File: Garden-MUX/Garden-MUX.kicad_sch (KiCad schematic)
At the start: 53 parts, among them J1 USB_C_Receptacle_USB2.0_16P, J2 SDCARD_MODULE, P1 S2B-PH-SM4-TB, Q1 AO3401A, U2 MCP73832-2-OT, U3 AP2112K-3.3, U4 AP2112K-3.3, U5 ESP32-C6-MINI-1

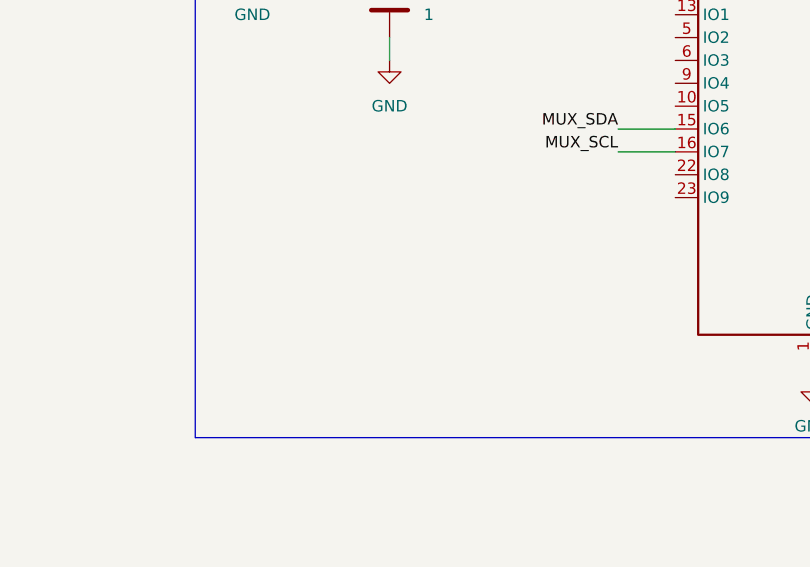
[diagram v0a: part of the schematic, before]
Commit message: Transfer capacitors from 4 layer board
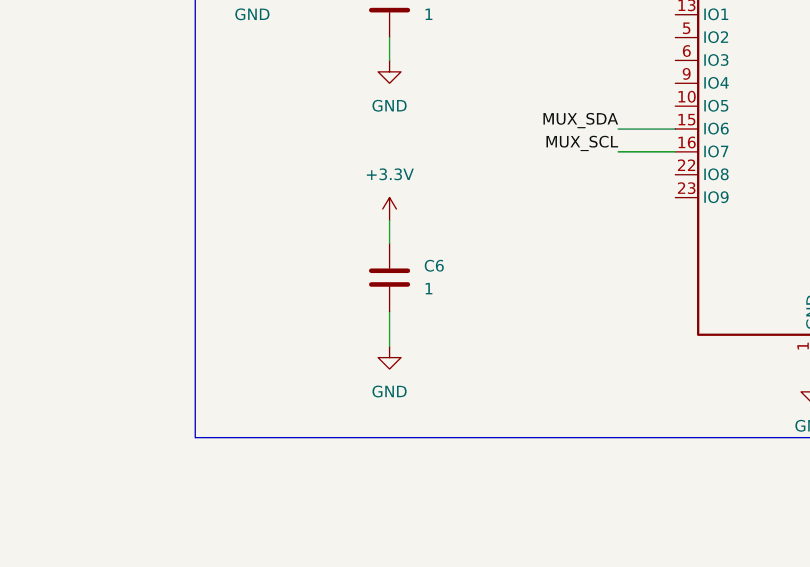
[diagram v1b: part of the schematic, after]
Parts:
- added C6: 1, Capacitor_SMD:C_0603_1608Metric, symbol Device:C
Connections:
- net +3.3V: now also C6.1
- net GND: now also C6.2
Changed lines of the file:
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@@
 	(wire
 		(pts
+			(xy 293.37 78.74) (xy 293.37 81.28)
+		)
+		(stroke
+			(width 0)
+			(type default)
+		)
+	)
+	(wire
+		(pts
 			(xy 417.83 58.42) (xy 417.83 68.58)
 		)
@@
 	(wire
 		(pts
+			(xy 293.37 88.9) (xy 293.37 92.71)
+		)
+		(stroke
+			(width 0)
+			(type default)
+		)
+	)
+	(wire
+		(pts
 			(xy 102.87 113.03) (xy 106.68 113.03)
 		)
@@
 	)
 	(symbol
+		(lib_id "power:GND")
+		(at 293.37 92.71 0)
+		(unit 1)
+		(exclude_from_sim no)
+		(in_bom yes)
+		(on_board yes)
+		(dnp no)
+		(fields_autoplaced yes)
+		(property "Reference" "#PWR039"
+			(at 293.37 99.06 0)
+			(effects
+				(font
+					(size 1.27 1.27)
+				)
+				(hide yes)
+			)
+		)
+		(property "Value" "GND"
+			(at 293.37 97.79 0)
+			(effects
+				(font
+					(size 1.27 1.27)
+				)
+			)
+		)
+		(property "Footprint" ""
+			(at 293.37 92.71 0)
+			(effects
+				(font
+					(size 1.27 1.27)
+				)
+				(hide yes)
+			)
+		)
+		(property "Datasheet" ""
+			(at 293.37 92.71 0)
+			(effects
+				(font
+					(size 1.27 1.27)
+				)
+				(hide yes)
+			)
+		)
+		(property "Description" "Power symbol creates a global label with name \"GND\" , ground"
+			(at 293.37 92.71 0)
+			(effects
+				(font
+					(size 1.27 1.27)
+				)
+				(hide yes)
+			)
+		)
+		(pin "1"
+		)
+		(instances
+			(project "Garden-MUX"
+				(path "/27ca7141-07bc-42d4-b74a-f55a9e480797"
+					(reference "#PWR039")
+					(unit 1)
+				)
+			)
+		)
+	)
+	(symbol
 		(lib_id "Mechanical:MountingHole")
 		(at 148.59 144.78 0)
@@
 	)
 	(symbol
+		(lib_id "power:+3V3")
+		(at 293.37 78.74 0)
+		(unit 1)
+		(exclude_from_sim no)
+		(in_bom yes)
+		(on_board yes)
+		(dnp no)
+		(fields_autoplaced yes)
+		(property "Reference" "#PWR040"
+			(at 293.37 82.55 0)
+			(effects
+				(font
+					(size 1.27 1.27)
+				)
+				(hide yes)
+			)
+		)
+		(property "Value" "+3.3V"
+			(at 293.37 73.66 0)
+			(effects
+				(font
+					(size 1.27 1.27)
+				)
+			)
+		)
+		(property "Footprint" ""
+			(at 293.37 78.74 0)
+			(effects
+				(font
+					(size 1.27 1.27)
+				)
+				(hide yes)
+			)
+		)
+		(property "Datasheet" ""
+			(at 293.37 78.74 0)
+			(effects
+				(font
+					(size 1.27 1.27)
+				)
+				(hide yes)
+			)
+		)
+		(property "Description" "Power symbol creates a global label with name \"+3V3\""
+			(at 293.37 78.74 0)
+			(effects
+				(font
+					(size 1.27 1.27)
+				)
+				(hide yes)
+			)
+		)
+		(pin "1"
+		)
+		(instances
+			(project "Garden-MUX"
+				(path "/27ca7141-07bc-42d4-b74a-f55a9e480797"
+					(reference "#PWR040")
+					(unit 1)
+				)
+			)
+		)
+	)
+	(symbol
 		(lib_id "power:GND")
 		(at 46.99 116.84 0)
@@
 					(unit 1)
 				)
+			)
+		)
+	)
+	(symbol
+		(lib_id "Device:C")
+		(at 293.37 85.09 0)
+		(unit 1)
+		(exclude_from_sim no)
+		(in_bom yes)
+		(on_board yes)
+		(dnp no)
+		(fields_autoplaced yes)
+		(property "Reference" "C6"
+			(at 297.18 83.8199 0)
+			(effects
+				(font
+					(size 1.27 1.27)
+				)
+				(justify left)
+			)
+		)
+		(property "Value" "1"
+			(at 297.18 86.3599 0)
+			(effects
+				(font
+					(size 1.27 1.27)
+				)
+				(justify left)
+			)
+		)
+		(property "Footprint" "Capacitor_SMD:C_0603_1608Metric"
+			(at 294.3352 88.9 0)
+			(effects
+				(font
+					(size 1.27 1.27)
+				)
+				(hide yes)
+			)
+		)
+		(property "Datasheet" "~"
+			(at 293.37 85.09 0)
+			(effects
+				(font
+					(size 1.27 1.27)
+				)
+				(hide yes)
+			)
+		)
+		(property "Description" "Unpolarized capacitor"
+			(at 293.37 85.09 0)
+			(effects
+				(font
+					(size 1.27 1.27)
+				)
+				(hide yes)
+			)
+		)
+		(pin "1"
+		)
+		(pin "2"
+		)
+		(instances
+			(project ""
+				(path "/27ca7141-07bc-42d4-b74a-f55a9e480797"
+					(reference "C6")
+					(unit 1)
+				)

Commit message: Update 3D models file locations to global
The 3D models file paths no longer need to modified to be seen
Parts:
- U5: footprint RF_Module:ESP32-C6-MINI-1 -> Pico_Footprints:ESP32-C6-MINI-1
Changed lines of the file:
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@@
 			)
 		)
-		(property "Footprint" "RF_Module:ESP32-C6-MINI-1"
+		(property "Footprint" "Pico_Footprints:ESP32-C6-MINI-1"
 			(at 358.14 93.98 0)
 			(effects

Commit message: Add boot button and adjust 3D models
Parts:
- added R2: 100k, Resistor_SMD:R_0603_1608Metric, symbol Device:R_US
- added S9: TL6330AF200Q, Pico_Footprints:SW_TL6330AF200Q_Footprint, symbol Pico_Symbols:TL6330AF200Q
- renumbered C23 to C10, C24 to C11, C25 to C12, C26 to C13, C19 to C7, C20 to C8, C21 to C9, R20 to R1, R12 to R10, R13 to R11, R14 to R12, R15 to R13, R16 to R14, R17 to R15, R18 to R16, R19 to R17, R2 to R3, R3 to R4, R4 to R5, R8 to R7, R10 to R8, R11 to R9, S11 to S10, U5 to U1
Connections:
- net +3.3V: now also R2.1
- net GND: now also S9.1, S9.2
- net BOOT: now reaches U1.23 (IO9)
- net BOOT: now also R2.2, S9.3, S9.4
- no-connect marks 3 -> 13
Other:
- moved on the sheet: C13, C5, C6, P1, R1, S10
